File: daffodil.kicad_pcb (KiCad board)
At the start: 2 copper layers, 70.7 x 53.3 mm, 8 parts, among them J1 NEIGHBOR1, J2 NEIGHBOR2, J7 BONUS_ROW, P1 GREATFET-PROTO-AREA

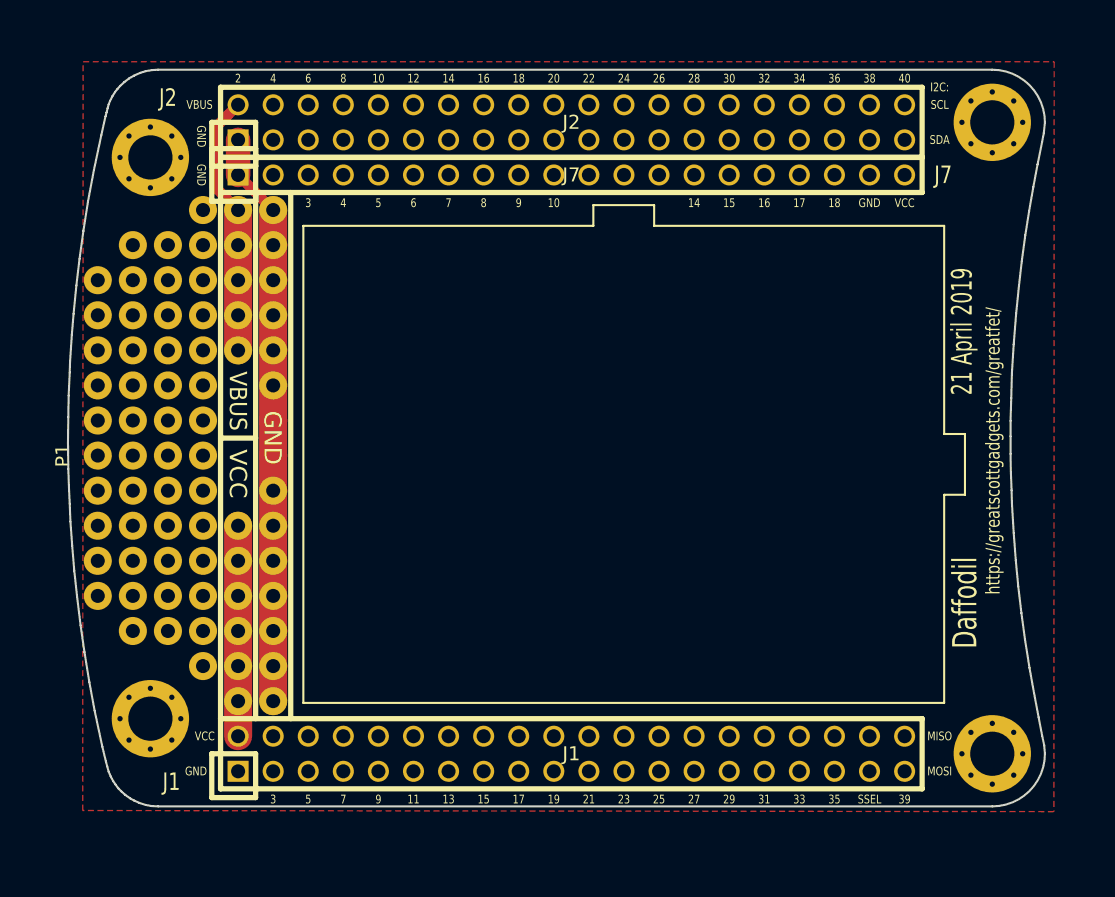
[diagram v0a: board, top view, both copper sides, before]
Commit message: voltage level shifter added
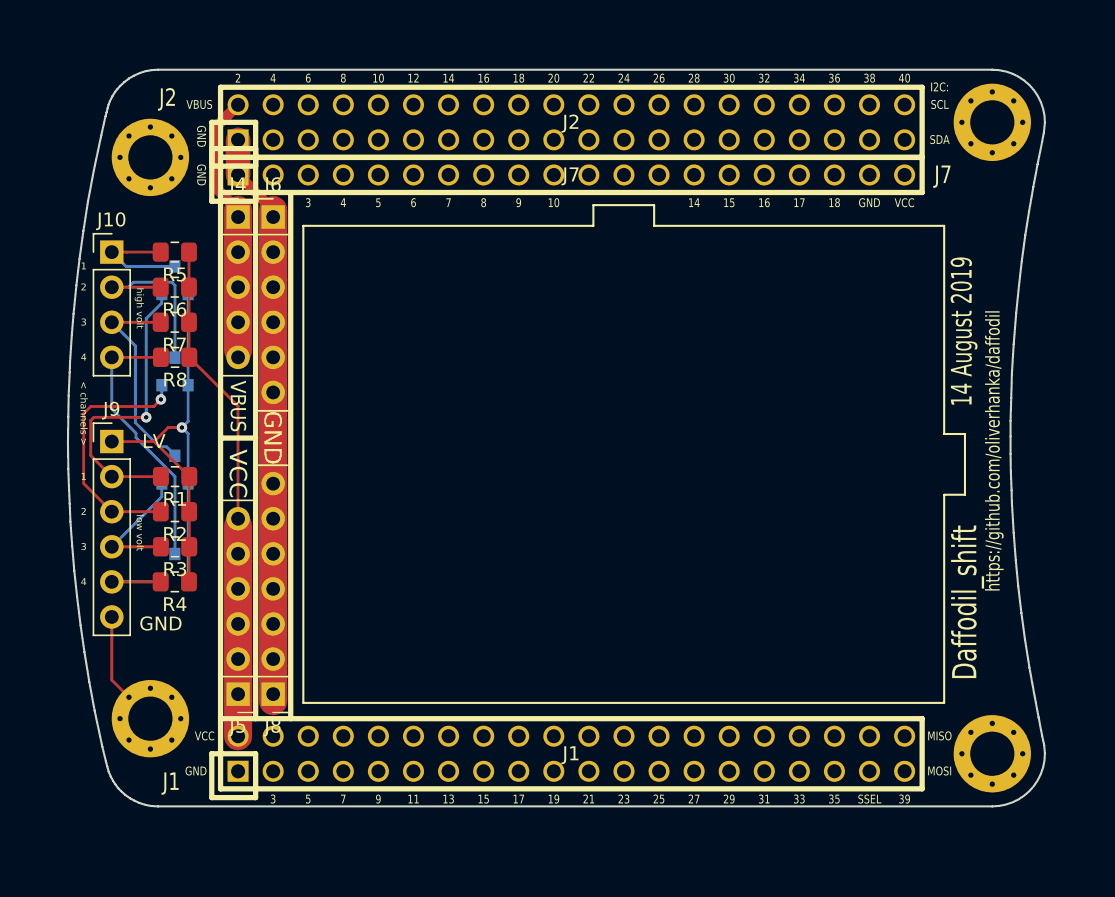
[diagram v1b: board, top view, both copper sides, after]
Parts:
- removed P1: GREATFET-PROTO-AREA, gsg-modules:GREATFET-PROTO-AREA
- added J10: Conn_01x04_Male, Connector_PinHeader_2.54mm:PinHeader_1x04_P2.54mm_Vertical, F.Cu at (112.8, 81.8)
- added J4: Conn_01x05_Male, Connector_PinHeader_2.54mm:PinHeader_1x05_P2.54mm_Vertical, F.Cu at (121.9, 79.2)
- added J5: Conn_01x06_Male, Connector_PinHeader_2.54mm:PinHeader_1x06_P2.54mm_Vertical, F.Cu at (121.9, 113.8)
- added J6: Conn_01x06_Male, Connector_PinHeader_2.54mm:PinHeader_1x06_P2.54mm_Vertical, F.Cu at (124.5, 79.2)
- added J8: Conn_01x07_Male, Connector_PinHeader_2.54mm:PinHeader_1x07_P2.54mm_Vertical, F.Cu at (124.5, 113.8)
- added J9: Conn_01x06_Male, Connector_PinHeader_2.54mm:PinHeader_1x06_P2.54mm_Vertical, F.Cu at (112.8, 95.5)
- added Q1: BSS138, Package_TO_SOT_SMD:SOT-23, B.Cu at (117.3, 83.8)
- added Q2: BSS138, Package_TO_SOT_SMD:SOT-23, B.Cu at (117.3, 90.4)
- added Q3: BSS138, Package_TO_SOT_SMD:SOT-23, B.Cu at (117.3, 97.5)
- added Q4: BSS138, Package_TO_SOT_SMD:SOT-23, B.Cu at (117.3, 104.6)
- added R1: 10k, Resistor_SMD:R_0805_2012Metric_Pad1.15x1.40mm_HandSolder, F.Cu at (117.4, 98.0)
- added R2: 10k, Resistor_SMD:R_0805_2012Metric_Pad1.15x1.40mm_HandSolder, F.Cu at (117.3, 100.6)
- added R3: 10k, Resistor_SMD:R_0805_2012Metric_Pad1.15x1.40mm_HandSolder, F.Cu at (117.4, 103.1)
- added R4: 10k, Resistor_SMD:R_0805_2012Metric_Pad1.15x1.40mm_HandSolder, F.Cu at (117.3, 105.7)
- added R5: 10k, Resistor_SMD:R_0805_2012Metric_Pad1.15x1.40mm_HandSolder, F.Cu at (117.3, 81.8)
- added R6: 10k, Resistor_SMD:R_0805_2012Metric_Pad1.15x1.40mm_HandSolder, F.Cu at (117.3, 84.3)
- added R7: 10k, Resistor_SMD:R_0805_2012Metric_Pad1.15x1.40mm_HandSolder, F.Cu at (117.3, 86.9)
- added R8: 10k, Resistor_SMD:R_0805_2012Metric_Pad1.15x1.40mm_HandSolder, F.Cu at (117.4, 89.4)
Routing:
- net +1V8: track 0.00 -> 37.9 mm, vias 0 -> 1
- net Net-(J9-Pad2): track 0.00 -> 21.8 mm, vias 0 -> 1
- net VCC: track 15.2 -> 36.0 mm
- net Net-(J10-Pad4): track 0.00 -> 19.7 mm
- net Net-(J9-Pad3): track 0.00 -> 18.6 mm, vias 0 -> 1
- net Net-(J10-Pad3): track 0.00 -> 15.4 mm
- net Net-(J10-Pad2): track 0.00 -> 13.6 mm
- net Net-(J9-Pad4): track 0.00 -> 9.64 mm
- net Net-(J10-Pad1): track 0.00 -> 8.54 mm
- net GND: track 41.7 -> 50.2 mm
- net Net-(J9-Pad5): track 0.00 -> 7.17 mm
- removed copper zone on F.Cu, net GND
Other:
- board text added: "1"
- board text added: "14 August 2019"
- board text added: "< channels >"
- board text added: "Daffodil_shift"
- board text added: "LV"
- board text added: "high volt"
- board text added: "https://github.com/oliverhanka/daffodil"
- board text added: "low volt"
- board text removed: "21 April 2019"
- board text removed: "Daffodil"
- board text removed: "https://greatscottgadgets.com/greatfet/"

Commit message: ground plane added
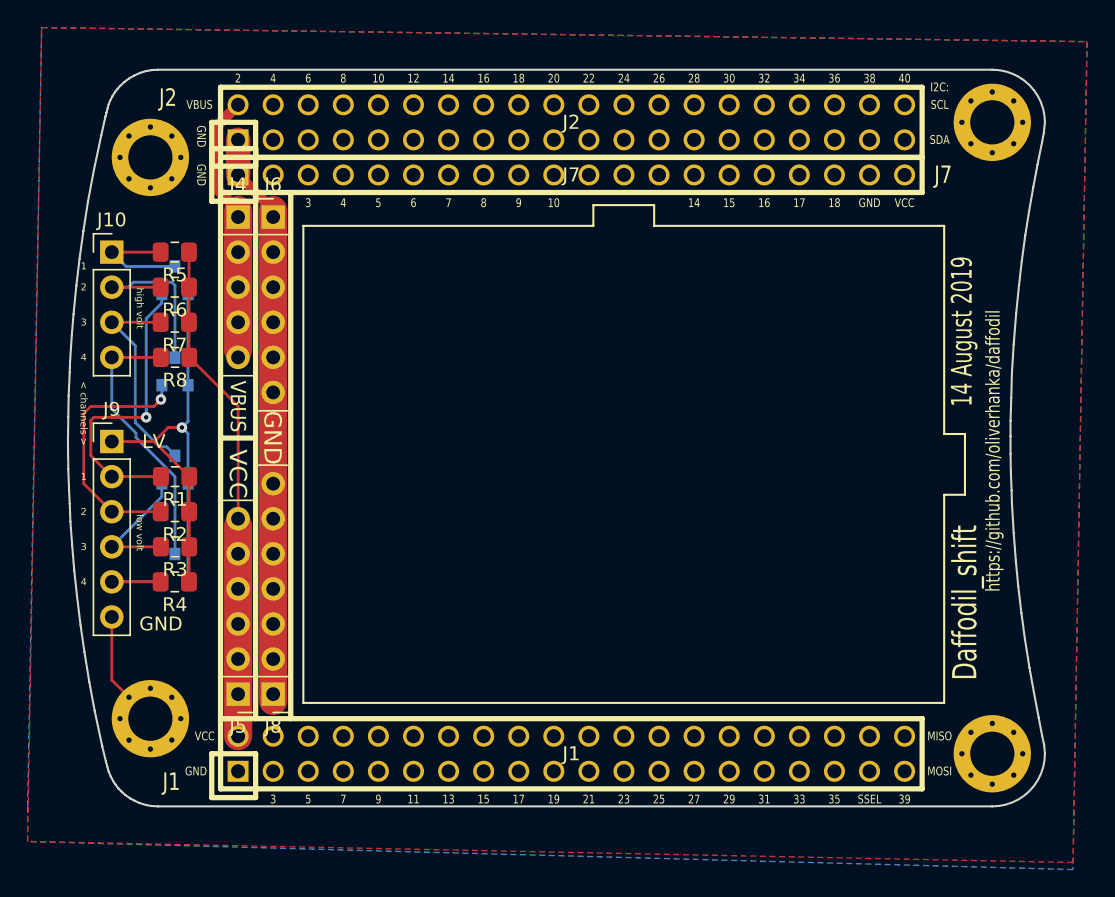
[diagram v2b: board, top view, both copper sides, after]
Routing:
- added copper zone on B.Cu, net GND
- added copper zone on F.Cu, net GND
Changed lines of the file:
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@@
+    )
+  )
+  (zone (net 1) (net_name GND) (layer F.Cu) (hatch edge 0.508)
+    (connect_pads (clearance 0.254))
+    (min_thickness 0.254)
+    (fill yes (arc_segments 32) (thermal_gap 0.508) (thermal_bridge_width 0.508))
+    (polygon
+      (pts
+        (xy 107.696 65.532) (xy 183.388 66.548) (xy 182.372 125.984) (xy 106.68 124.46)
+      )
+    )
+  )
+  (zone (net 1) (net_name GND) (layer B.Cu) (hatch edge 0.508)
+    (connect_pads (clearance 0.254))
+    (min_thickness 0.254)
+    (fill yes (arc_segments 32) (thermal_gap 0.508) (thermal_bridge_width 0.508))
+    (polygon
+      (pts
+        (xy 107.696 65.532) (xy 183.388 66.548) (xy 182.372 126.492) (xy 106.68 124.46) (xy 106.68 121.92)
+      )
     )
   )
